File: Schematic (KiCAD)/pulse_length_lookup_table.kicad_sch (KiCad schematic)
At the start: 121 parts

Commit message: - Pulse DAC logic is now complete.  - The 4-bit adders are verified correct using Excel.    - This revealed 1 tracing error and also 3 XNOR gates that are actually XOR in this case.  - Now including a PDF version of the schematic.
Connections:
- net at B108. (X): now also A78. (X); no longer A70. (X)
- net at A71. (X): now also A72. (X), A73. (X); no longer A70. (X)
- net at C16. (X): now also D47. (X); no longer C15. (X)
- net at D45. (X): now also D46. (X); no longer C16. (X)
- net at D47. (X): now also D48. (X); no longer C16. (X)
- net at D72. (X): now also C22. (X); no longer D71. (X)
- net at D92. (X): now also C26. (X); no longer D91. (X)
- net at C26. (X): now also C25. (X); no longer D92. (X)
- net at C18. (X): now also D51. (X); no longer C17. (X)
- net at D106. (X): now also C28. (X); no longer D105. (X)
- net at A58. (X): now also A57. (X), A66. (/Q7); no longer A59. (X)
- net at D66. (X): now also D65. (X); no longer C20. (X)
- net at A67. (/Q4): now also A65. (X)
- net at A66.7. (X): now also A66.4. (X); no longer A67. (/Q4)
- net at A68. (X): now also A66.4. (X); no longer A67. (/Q4)
- net at A66.6. (X): now also A66.4. (X); no longer A67. (/Q4)
- net at A69. (X): now also A77. (X); no longer A67. (/Q4)
- net at A65. (X): now also A64. (X); no longer A67. (/Q4)
- net at A66.4. (X): now also A66.5. (X), A78. (X); no longer A66.7. (X)
- net at D64. (X): now also C20. (X); no longer D63. (X)
- net at D76. (X): now also C22. (X); no longer D75. (X)
- net at D53. (X): now also C18. (X); no longer D54. (X)
- net at D96. (X): now also D95. (X); no longer C26. (X)
- net at A73. (X): now also A74. (X); no longer A82. (X)
- net at A74. (X): now also A75. (X); no longer A73. (X)
- net at D49. (X): now also C18. (X); no longer D50. (X)
- net at D55. (X): now also C18. (X); no longer D56. (X)
- net at D74. (X): now also D73. (X); no longer C22. (X)
- net at D70. (X): now also D69. (X); no longer C22. (X)
- net at D68. (X): now also D67. (X); no longer C22. (X)
- net at A77. (X): now also A82. (X); no longer A81. (X)
- net at A77. (X), A80. (X): now also A79. (X)
- net at D104. (X): now also C28. (X); no longer D103. (X)
- net at C28. (X): now also C27. (X); no longer D104. (X)
- net at D58. (X): now also C20. (X); no longer D57. (X)
- net at C20. (X): now also D62. (X); no longer D58. (X)
- net at A66.3. (X): now also A66. (/Q7); no longer A66.4. (X)
- net at D78. (X): now also C24. (X); no longer D77. (X)
- net at C24. (X): now also D88. (X); no longer D78. (X)
- net at B43. (X): now also B42. (X)
- net at D102. (X): now also C28. (X); no longer D101. (X)
- net at C9. (X): now also C8. (X); no longer C10. (X)
- net at D51. (X): now also D52. (X); no longer C18. (X)
- net at D100. (X): now also C26. (X); no longer D99. (X)
- net at D60. (X): now also C20. (X); no longer D59. (X)
- net at D84. (X): now also D83. (X); no longer C24. (X)
- net at D86. (X): now also C24. (X); no longer D85. (X)
- net at D82. (X): now also D81. (X); no longer C24. (X)
- net at D80. (X): now also D79. (X); no longer C24. (X)
- net at D90. (X): now also C26. (X); no longer D89. (X)
- net at A66.2. (X): now also A66. (/Q7); no longer A66.5. (X)
- net at A60. (X): now also A56. (X); no longer A61. (X)
- net at D94. (X): now also C26. (X); no longer D93. (X)
- net at D98. (X): now also D97. (X); no longer C26. (X)
- new net: A70. (X), B108. (X)
- new net: A70. (X), A71. (X)
- new net: C15. (X), C16. (X)
- new net: C16. (X), D45. (X)
- new net: D71. (X), D72. (X)
- new net: D91. (X), D92. (X)
- new net: C17. (X), C18. (X)
- new net: D105. (X), D106. (X)
- new net: A58. (X), A59. (X)
- new net: C20. (X), D66. (X)
- new net: A66.7. (X), A67. (/Q4)
- new net: A67. (/Q4), A68. (X)
- new net: A66.6. (X), A67. (/Q4)
- new net: A67. (/Q4), A69. (X)
- new net: A66. (/Q7), A67. (/Q4)
- new net: D63. (X), D64. (X)
- new net: D75. (X), D76. (X)
- new net: D53. (X), D54. (X)
- new net: C26. (X), D96. (X)
- new net: A73. (X), A82. (X)
- new net: D49. (X), D50. (X)
- new net: A64. (X), A66.4. (X), A66.5. (X)
- new net: D55. (X), D56. (X)
- new net: C21. (X), C22. (X)
- new net: C22. (X), D74. (X)
- new net: C22. (X), D70. (X)
- new net: C22. (X), D68. (X)
- new net: A77. (X), A81. (X)
- new net: A77. (X), A80. (X)
- new net: D103. (X), D104. (X)
- new net: D57. (X), D58. (X)
- new net: D61. (X), D62. (X)
- new net: A66.3. (X), A66.4. (X)
- new net: D77. (X), D78. (X)
- new net: C23. (X), C24. (X)
- new net: C19. (X), C20. (X)
- new net: A55. (/Q), A56. (X), A57. (X)
- new net: B43. (X), B44. (X)
- new net: D101. (X), D102. (X)
- new net: C10. (X), D38. (Ripple_Out)
- new net: C10. (X), C9. (X)
- new net: D100. (X), D99. (X)
- new net: D59. (X), D60. (X)
- new net: D38. (Ripple_Out), D39. (Ripple_Out)
- new net: C24. (X), D84. (X)
- new net: D85. (X), D86. (X)
- new net: C11. (Ripple_Out), C12. (Ripple_Out)
- new net: B42. (X), C11. (Ripple_Out)
- new net: D87. (X), D88. (X)
- new net: C24. (X), D82. (X)
- new net: C24. (X), D80. (X)
- new net: D89. (X), D90. (X)
- new net: A66.2. (X), A66.5. (X)
- new net: A60. (X), A61. (X)
- new net: D93. (X), D94. (X)
- new net: A78. (X), A83. (X), B107. (X)
- new net: C26. (X), D98. (X)

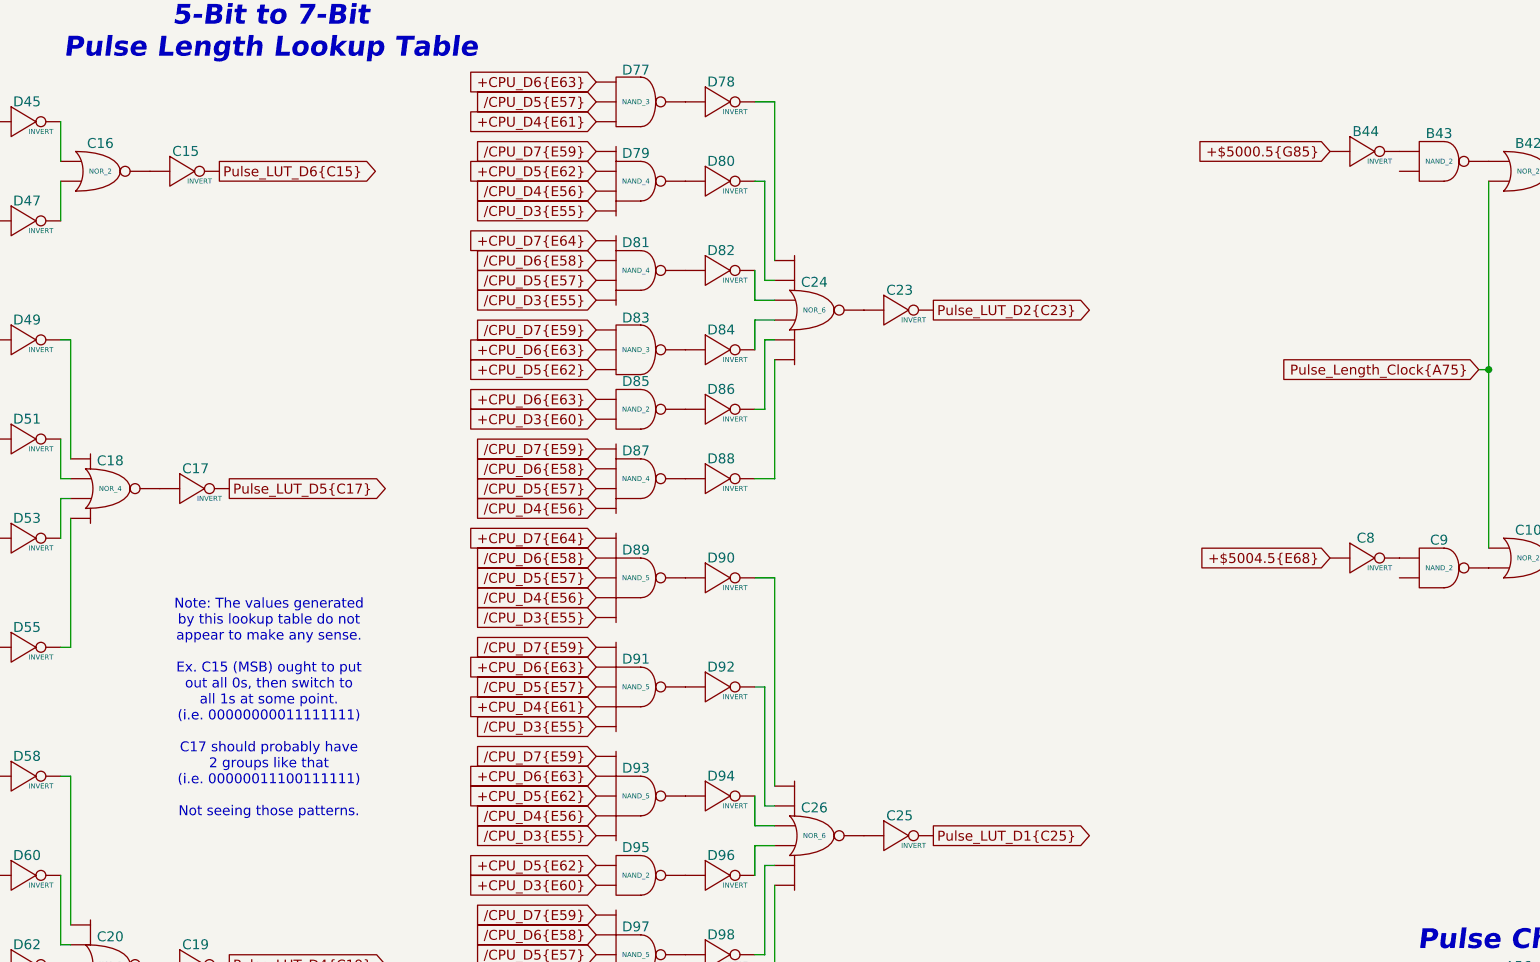
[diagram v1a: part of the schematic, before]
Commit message: Schematic Updates:  - Added all 10-bit CHR banking registers $5120 - $512B, including where all 10 bits come from when written.  - Added 8-bit CHR bank register $5202, which is the bank used when rendering the V-Split region.    + V-Split seems to always be 8-bit, 8kB bank regardless of CHR mode.  The wiki doesn't say that and I don't know for sure.  - Added decoding logic that activates the correct CHR bank for CHR A10, A11, A12 (corresponding to columns AV, AW, AX).  - Noted, AX15 activates $5202 CHR Bank for V-Split region.  AX16 activates CHR Bank from data stored in ExRAM for extended attributes.  Therefore, AX15 driven by AT1 High means we specifically are in v-split region, and not extended attribute mode.  With this knowledge, backtracking up the chain from AT1 to N14 sheds very useful insight what the 3-bit shift register at N11/N12/N13 is doing.  We now know that N14 goes low specifically for pattern table fetches when rendering the V-split region, and does not appear dual-purposed for extended attribute fetch sequencing.  This may seem rather subtle or unimportant, but it is a good advancement for higher level understanding what that mysterious shift register might be doing.
SVG Trace Updates:
 - Registers $5120, 5121, 5122, 5123 (first 4 CHR bank register), the outputs were labeled in reverse order.
 - Register $5130 (highest CHR bank bits), the outputs were labeled with backwards polarity.  The error was not having taken into account that the CPU data bus input to the latches came already inverted to begin with.
 - Still wrong: Cell AV7, 2-input NAND gate.  One of the inputs is missing and it logically should be driven by AS19 like the 4 cells to its direct right.  I can't quite make out how it makes that connection.
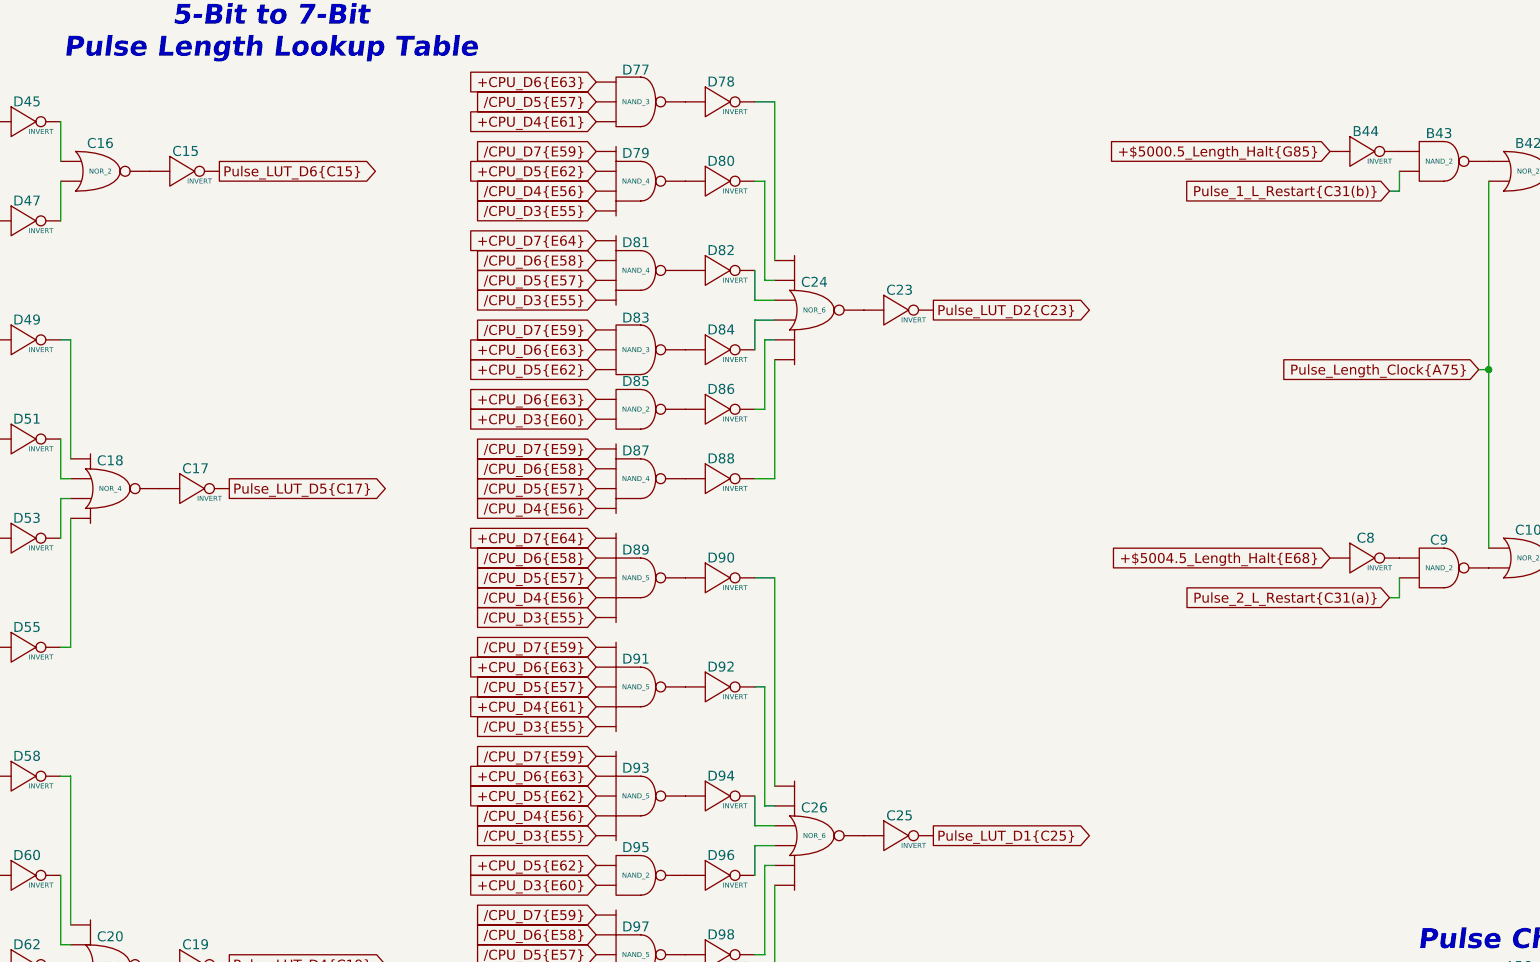
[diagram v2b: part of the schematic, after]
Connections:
- net +$5000.5{G85} is gone; now on net +$5000.5_Length_Halt{G85}: B44. (X)
- net +$5004.5{E68} is gone; now on net +$5004.5_Length_Halt{E68}: C8. (X)
- net at B108. (X): now also A78. (X); no longer A70. (X)
- net at A71. (X): now also A72. (X), A73. (X); no longer A70. (X)
- net at C16. (X): now also D47. (X); no longer C15. (X)
- net at D45. (X): now also D46. (X); no longer C16. (X)
- net at D47. (X): now also D48. (X); no longer C16. (X)
- net at D72. (X): now also C22. (X); no longer D71. (X)
- net at D92. (X): now also C26. (X); no longer D91. (X)
- net at C26. (X): now also C25. (X); no longer D92. (X)
- net at C18. (X): now also D51. (X); no longer C17. (X)
- net at D106. (X): now also C28. (X); no longer D105. (X)
- net at A58. (X): now also A57. (X), A66. (/Q7); no longer A59. (X)
- net at D66. (X): now also D65. (X); no longer C20. (X)
- net at A67. (/Q4): now also A65. (X)
- net at A66.7. (X): now also A66.4. (X); no longer A67. (/Q4)
- net at A68. (X): now also A66.4. (X); no longer A67. (/Q4)
- net at A66.6. (X): now also A66.4. (X); no longer A67. (/Q4)
- net at A69. (X): now also A77. (X); no longer A67. (/Q4)
- net at A65. (X): now also A64. (X); no longer A67. (/Q4)
- net at A66.4. (X): now also A66.5. (X), A78. (X); no longer A66.7. (X)
- net at D64. (X): now also C20. (X); no longer D63. (X)
- net at D76. (X): now also C22. (X); no longer D75. (X)
- net at D53. (X): now also C18. (X); no longer D54. (X)
- net at D96. (X): now also D95. (X); no longer C26. (X)
- net at A73. (X): now also A74. (X); no longer A82. (X)
- net at A74. (X): now also A75. (X); no longer A73. (X)
- net at D49. (X): now also C18. (X); no longer D50. (X)
- net at D55. (X): now also C18. (X); no longer D56. (X)
- net at D74. (X): now also D73. (X); no longer C22. (X)
- net at D70. (X): now also D69. (X); no longer C22. (X)
- net at D68. (X): now also D67. (X); no longer C22. (X)
- net at A77. (X): now also A82. (X); no longer A81. (X)
- net at A77. (X), A80. (X): now also A79. (X)
- net at D104. (X): now also C28. (X); no longer D103. (X)
- net at C28. (X): now also C27. (X); no longer D104. (X)
- net at D58. (X): now also C20. (X); no longer D57. (X)
- net at C20. (X): now also D62. (X); no longer D58. (X)
- net at A66.3. (X): now also A66. (/Q7); no longer A66.4. (X)
- net at D78. (X): now also C24. (X); no longer D77. (X)
- net at C24. (X): now also D88. (X); no longer D78. (X)
- net Pulse_1_L_Restart{C31(b)}: now reaches B43. (X)
- net +$5000.5_Length_Halt{G85}: now reaches B44. (X)
- net +$5000.5_Length_Halt{G85}: no longer B43. (X)
- net at D102. (X): now also C28. (X); no longer D101. (X)
- net Pulse_2_L_Restart{C31(a)}: now reaches C9. (X)
- net Pulse_2_L_Restart{C31(a)}: no longer C10. (X)
- net at D51. (X): now also D52. (X); no longer C18. (X)
- net at D100. (X): now also C26. (X); no longer D99. (X)
- net at D60. (X): now also C20. (X); no longer D59. (X)
- net at D84. (X): now also D83. (X); no longer C24. (X)
- net at D86. (X): now also C24. (X); no longer D85. (X)
- net at D82. (X): now also D81. (X); no longer C24. (X)
- net at D80. (X): now also D79. (X); no longer C24. (X)
- net at D90. (X): now also C26. (X); no longer D89. (X)
- net at A66.2. (X): now also A66. (/Q7); no longer A66.5. (X)
- net +$5004.5_Length_Halt{E68}: now reaches C8. (X)
- net +$5004.5_Length_Halt{E68}: no longer C9. (X)
- net at A60. (X): now also A56. (X); no longer A61. (X)
- net at D94. (X): now also C26. (X); no longer D93. (X)
- net at D98. (X): now also D97. (X); no longer C26. (X)
- new net: A70. (X), B108. (X)
- new net: A70. (X), A71. (X)
- new net: C15. (X), C16. (X)
- new net: C16. (X), D45. (X)
- new net: D71. (X), D72. (X)
- new net: D91. (X), D92. (X)
- new net: C17. (X), C18. (X)
- new net: D105. (X), D106. (X)
- new net: A58. (X), A59. (X)
- new net: C20. (X), D66. (X)
- new net: A66.7. (X), A67. (/Q4)
- new net: A67. (/Q4), A68. (X)
- new net: A66.6. (X), A67. (/Q4)
- new net: A67. (/Q4), A69. (X)
- new net: A66. (/Q7), A67. (/Q4)
- new net: D63. (X), D64. (X)
- new net: D75. (X), D76. (X)
- new net: D53. (X), D54. (X)
- new net: C26. (X), D96. (X)
- new net: A73. (X), A82. (X)
- new net: D49. (X), D50. (X)
- new net: A64. (X), A66.4. (X), A66.5. (X)
- new net: D55. (X), D56. (X)
- new net: C21. (X), C22. (X)
- new net: C22. (X), D74. (X)
- new net: C22. (X), D70. (X)
- new net: C22. (X), D68. (X)
- new net: A77. (X), A81. (X)
- new net: A77. (X), A80. (X)
- new net: D103. (X), D104. (X)
- new net: D57. (X), D58. (X)
- new net: D61. (X), D62. (X)
- new net: A66.3. (X), A66.4. (X)
- new net: D77. (X), D78. (X)
- new net: C23. (X), C24. (X)
- new net: C19. (X), C20. (X)
- new net: A55. (/Q), A56. (X), A57. (X)
- new net: B43. (X), B44. (X)
- new net: B42. (X), B43. (X)
- new net: D101. (X), D102. (X)
- new net: C10. (X), D38. (Ripple_Out)
- new net: C10. (X), C9. (X)
- new net: D100. (X), D99. (X)
- new net: D59. (X), D60. (X)
- new net: D38. (Ripple_Out), D39. (Ripple_Out)
- new net: C24. (X), D84. (X)
- new net: D85. (X), D86. (X)
- new net: C11. (Ripple_Out), C12. (Ripple_Out)
- new net: B42. (X), C11. (Ripple_Out)
- new net: D87. (X), D88. (X)
- new net: C24. (X), D82. (X)
- new net: C24. (X), D80. (X)
- new net: D89. (X), D90. (X)
- new net: A66.2. (X), A66.5. (X)
- new net: C8. (X), C9. (X)
- new net: A60. (X), A61. (X)
- new net: D93. (X), D94. (X)
- new net: A78. (X), A83. (X), B107. (X)
- new net: C26. (X), D98. (X)
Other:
- note removed: "Note: The values generated by this lookup table do not appear to make any sense. Ex. C15 (MSB) ought to put out all 0s, then switch to all 1s at some point. (i.e. 00000000011111111) C17 should probably have 2 groups like that (i.e. 00000011100111111) Not seeing those patterns."
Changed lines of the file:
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@@
 		)
 	)
-	(text "Note: The values generated\nby this lookup table do not\nappear to make any sense.\n\nEx. C15 (MSB) ought to put\nout all 0s, then switch to\nall 1s at some point.\n(i.e. 00000000011111111)\n\nC17 should probably have\n2 groups like that\n(i.e. 00000011100111111)\n\nNot seeing those patterns."
-		(exclude_from_sim no)
-		(at 81.28 106.934 0)
-		(effects
-			(font
-				(size 1.27 1.27)
-			)
-		)
-	)
 	(junction
 		(at 270.51 232.41)
@@
 	(wire
 		(pts
+			(xy 226.06 92.71) (xy 226.06 90.17)
+		)
+		(stroke
+			(width 0)
+			(type default)
+		)
+	)
+	(wire
+		(pts
 			(xy 288.29 187.96) (xy 288.29 207.01)
 		)
@@
 	(wire
 		(pts
+			(xy 224.79 92.71) (xy 226.06 92.71)
+		)
+		(stroke
+			(width 0)
+			(type default)
+		)
+	)
+	(wire
+		(pts
 			(xy 213.36 199.39) (xy 213.36 207.01)
 		)
@@
 	(wire
 		(pts
+			(xy 226.06 40.64) (xy 226.06 38.1)
+		)
+		(stroke
+			(width 0)
+			(type default)
+		)
+	)
+	(wire
+		(pts
 			(xy 269.24 110.49) (xy 273.05 110.49)
 		)
@@
 		)
 	)
+	(wire
+		(pts
+			(xy 224.79 40.64) (xy 226.06 40.64)
+		)
+		(stroke
+			(width 0)
+			(type default)
+		)
+	)
 	(global_label "Pulse_LUT_D5{C17}"
 		(shape input)
@@
 		)
 	)
-	(global_label "+$5004.5{E68}"
+	(global_label "+$5004.5_Length_Halt{E68}"
 		(shape input)
 		(at 217.17 87.63 180)
@@
 		)
 		(property "Intersheetrefs" "${INTERSHEET_REFS}"
-			(at 199.4892 87.63 0)
+			(at 187.3942 87.63 0)
 			(effects
 				(font
@@
 		)
 	)
-	(global_label "+$5000.5{G85}"
+	(global_label "+$5000.5_Length_Halt{G85}"
 		(shape input)
 		(at 217.17 35.56 180)
@@
 		)
 		(property "Intersheetrefs" "${INTERSHEET_REFS}"
-			(at 199.3682 35.56 0)
+			(at 187.2732 35.56 0)
 			(effects
 				(font
@@
 		)
 	)
+	(global_label "Pulse_1_L_Restart{C31(b)}"
+		(shape input)
+		(at 224.79 40.64 180)
+		(fields_autoplaced yes)
+		(effects
+			(font
+				(size 1.27 1.27)
+			)
+			(justify right)
+		)
+		(property "Intersheetrefs" "${INTERSHEET_REFS}"
+			(at 196.4654 40.64 0)
+			(effects
+				(font
+					(size 1.27 1.27)
+				)
+				(justify right)
+				(hide yes)
+			)
+		)
+	)
 	(global_label "{slash}CPU_D7{E59}"
 		(shape input)
@@
 			(effects
 				(font
+					(size 1.27 1.27)
+				)
+				(justify right)
+				(hide yes)
+			)
+		)
+	)
+	(global_label "Pulse_2_L_Restart{C31(a)}"
+		(shape input)
+		(at 224.79 92.71 180)
+		(fields_autoplaced yes)
+		(effects
+			(font
+				(size 1.27 1.27)
+			)
+			(justify right)
+		)
+		(property "Intersheetrefs" "${INTERSHEET_REFS}"
+			(at 196.4654 92.71 0)
+			(effects
+				(font
